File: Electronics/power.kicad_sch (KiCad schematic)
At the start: 17 parts, among them J5 Conn_02x08_Odd_Even, U1 TL072

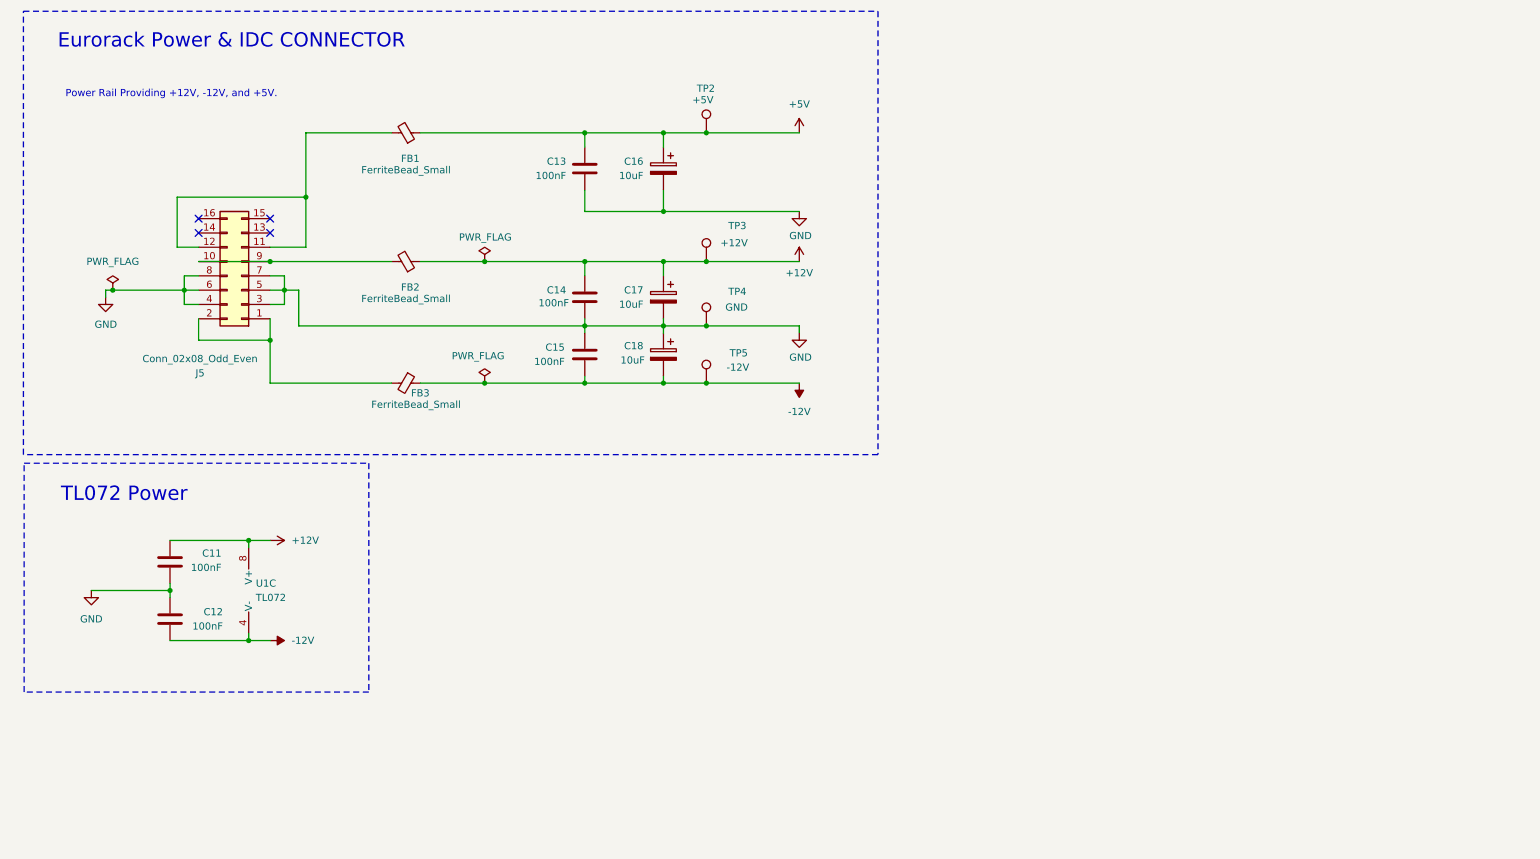
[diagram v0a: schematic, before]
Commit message: creating a 6HP PCB panel
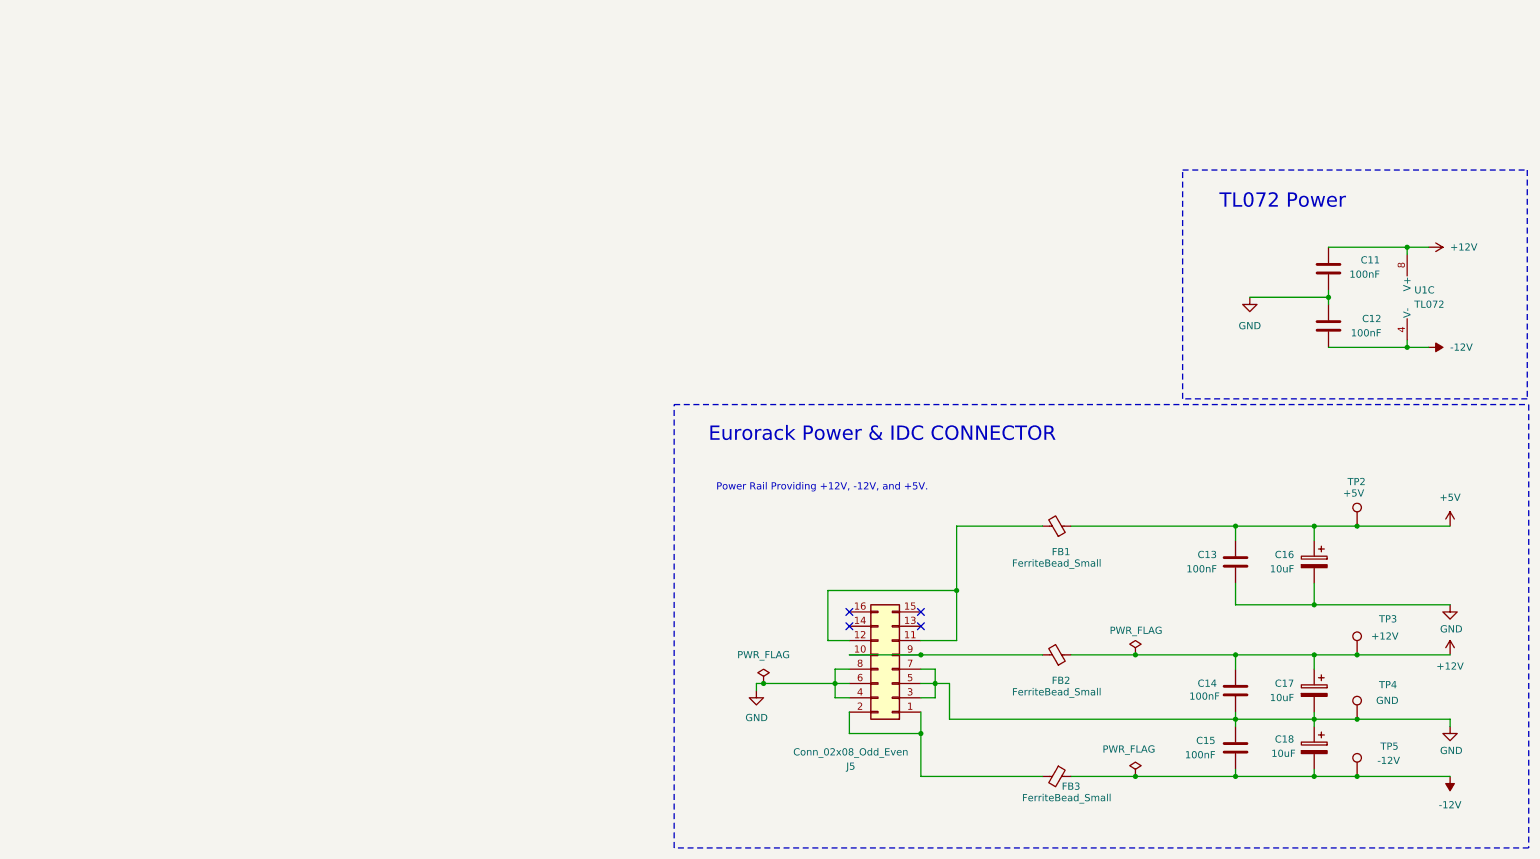
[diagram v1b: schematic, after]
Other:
- moved on the sheet: C11, C12, C13, C14, C15, C16, C17, C18, FB1, FB2, FB3, J5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
